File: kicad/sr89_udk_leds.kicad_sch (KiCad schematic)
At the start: 130 parts

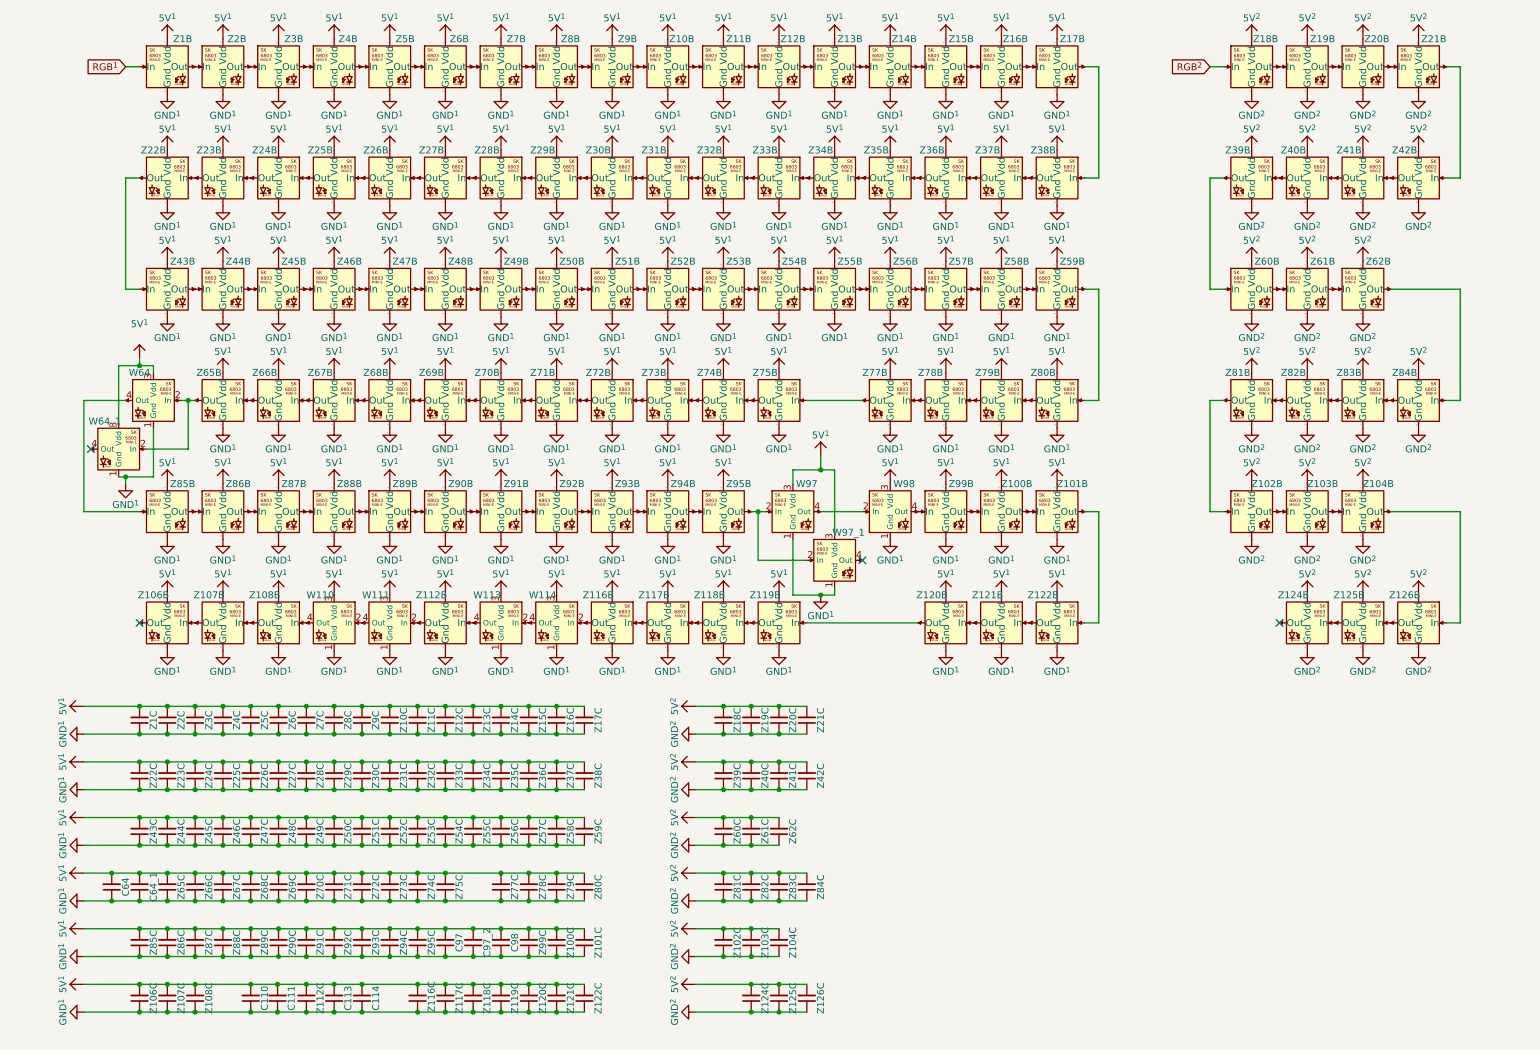
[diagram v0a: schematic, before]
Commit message: routed, but not rules checked
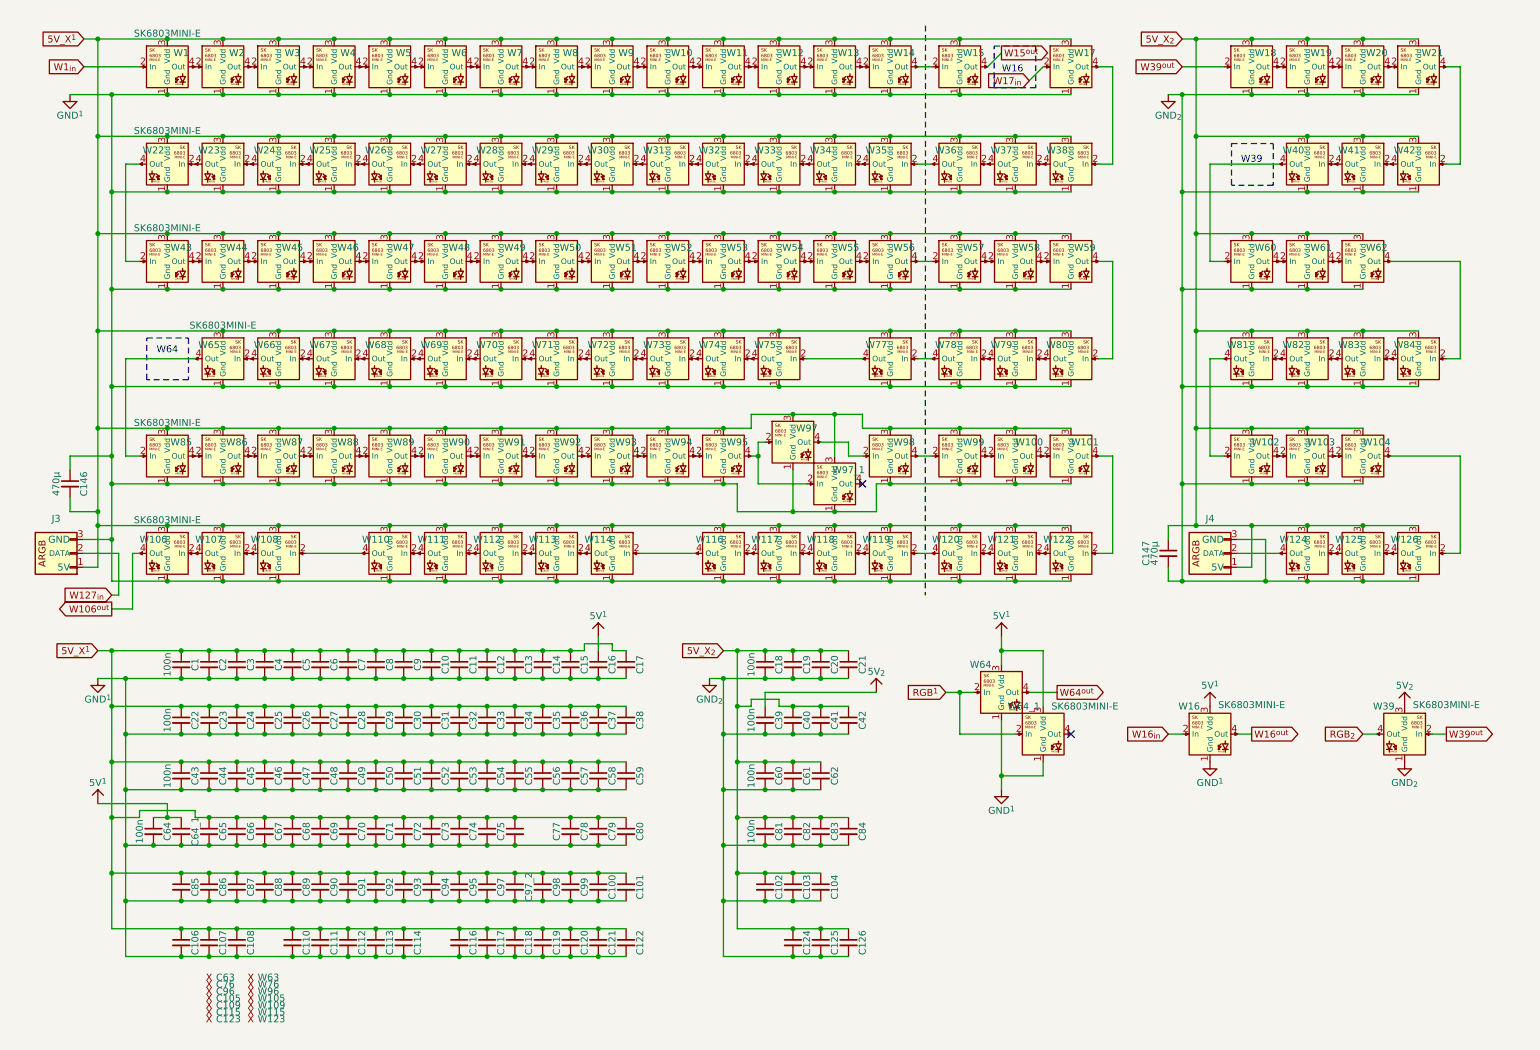
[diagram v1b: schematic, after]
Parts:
- removed Z1, Z10, Z100, Z101, Z102, Z103, Z104, Z106, Z107, Z108, Z11, Z112, Z116, Z117, Z118, Z119, Z12, Z120, Z121, Z122, Z124, Z125, Z126, Z13, Z14, Z15, Z16, Z17, Z18, Z19, Z2, Z20, Z21, Z22, Z23, Z24, Z25, Z26, Z27, Z28, Z29, Z3, Z30, Z31, Z32, Z33, Z34, Z35, Z36, Z37, Z38, Z39, Z4, Z40, Z41, Z42, Z43, Z44, Z45, Z46, Z47, Z48, Z49, Z5, Z50, Z51, Z52, Z53, Z54, Z55, Z56, Z57, Z58, Z59, Z6, Z60, Z61, Z62, Z65, Z66, Z67, Z68, Z69, Z7, Z70, Z71, Z72, Z73, Z74, Z75, Z77, Z78, Z79, Z8, Z80, Z81, Z82, Z83, Z84, Z85, Z86, Z87, Z88, Z89, Z9, Z90, Z91, Z92, Z93, Z94, Z95, Z99: (no value), 0_sr89:Combined_SW_1, symbol 0_sr89:Combined_SW
- added C1, C10, C100, C101, C102, C103, C104, C106, C107, C108, C11, C112, C116, C117, C118, C119, C12, C120, C121, C122, C124, C125, C126, C13, C14, C15, C16, C17, C18, C19, C2, C20, C21, C22, C23, C24, C25, C26, C27, C28, C29, C3, C30, C31, C32, C33, C34, C35, C36, C37, C38, C39, C4, C40, C41, C42, C43, C44, C45, C46, C47, C48, C49, C5, C50, C51, C52, C53, C54, C55, C56, C57, C58, C59, C6, C60, C61, C62, C65, C66, C67, C68, C69, C7, C70, C71, C72, C73, C74, C75, C77, C78, C79, C8, C80, C81, C82, C83, C84, C85, C86, C87, C88, C89, C9, C90, C91, C92, C93, C94, C95, C99: 100n, Capacitor_SMD:C_0402_1005Metric, symbol ts-kicad-lib:C
- added C105, C109, C115, C123, C63, C76, C96, W105, W109, W115, W123, W63, W76, W96: (no value), symbol 0_sr89:X
- added C146, C147: 470µ, Capacitor_SMD:C_0603_1608Metric, symbol ts-kicad-lib:C
- added J3, J4: (no value), ts-kicad-lib:JRAINBOW-5V-ARGB, symbol ts-kicad-lib:ARGB-5V-HEADER
- added W1, W10, W100, W101, W102, W103, W104, W106, W107, W108, W11, W112, W116, W117, W118, W119, W12, W120, W121, W122, W124, W125, W126, W13, W14, W15, W16, W17, W18, W19, W2, W20, W21, W22, W23, W24, W25, W26, W27, W28, W29, W3, W30, W31, W32, W33, W34, W35, W36, W37, W38, W39, W4, W40, W41, W42, W43, W44, W45, W46, W47, W48, W49, W5, W50, W51, W52, W53, W54, W55, W56, W57, W58, W59, W6, W60, W61, W62, W65, W66, W67, W68, W69, W7, W70, W71, W72, W73, W74, W75, W77, W78, W79, W8, W80, W81, W82, W83, W84, W85, W86, W87, W88, W89, W9, W90, W91, W92, W93, W94, W95, W99: SK6803MINI-E, ts-keyboard-lib:SK6803MINI-E, symbol ts-keyboard-lib:SK6803MINI-E
- C64, C64_1: value (none) -> 100n
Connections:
- net 5V^{1}: now also C64.1, C64_1.1, C16.1, W16.3 (Vdd); no longer C110.2, C111.2, C113.2, C114.2, C64.2, C64_1.2, C97.2, C97_2.2, C98.2, W110.3 (Vdd), W111.3 (Vdd), W113.3 (Vdd), W114.3 (Vdd), W97.3 (Vdd), W97_1.3 (Vdd), W98.3 (Vdd)
- net GND^{1}: now also C110.2, C111.2, C113.2, C114.2, C64.2, C64_1.2, C97.2, C97_2.2, C98.2, C1.2, C10.2, C100.2, C101.2, C106.2, C107.2, C108.2, C11.2, C112.2, C116.2, C117.2, C118.2, C119.2, C12.2, C120.2, C121.2, C122.2, C13.2, C14.2, C146.1, C15.2, C16.2, C17.2, C2.2, C22.2, C23.2, C24.2, C25.2, C26.2, C27.2, C28.2, C29.2, C3.2, C30.2, C31.2, C32.2, C33.2, C34.2, C35.2, C36.2, C37.2, C38.2, C4.2, C43.2, C44.2, C45.2, C46.2, C47.2, C48.2, C49.2, C5.2, C50.2, C51.2, C52.2, C53.2, C54.2, C55.2, C56.2, C57.2, C58.2, C59.2, C6.2, C65.2, C66.2, C67.2, C68.2, C69.2, C7.2, C70.2, C71.2, C72.2, C73.2, C74.2, C75.2, C77.2, C78.2, C79.2, C8.2, C80.2, C85.2, C86.2, C87.2, C88.2, C89.2, C9.2, C90.2, C91.2, C92.2, C93.2, C94.2, C95.2, C99.2, J3.3 (GND), W1.1 (Gnd), W10.1 (Gnd), W100.1 (Gnd), W101.1 (Gnd), W106.1 (Gnd), W107.1 (Gnd), W108.1 (Gnd), W11.1 (Gnd), W112.1 (Gnd), W116.1 (Gnd), W117.1 (Gnd), W118.1 (Gnd), W119.1 (Gnd), W12.1 (Gnd), W120.1 (Gnd), W121.1 (Gnd), W122.1 (Gnd), W13.1 (Gnd), W14.1 (Gnd), W15.1 (Gnd), W16.1 (Gnd), W17.1 (Gnd), W2.1 (Gnd), W22.1 (Gnd), W23.1 (Gnd), W24.1 (Gnd), W25.1 (Gnd), W26.1 (Gnd), W27.1 (Gnd), W28.1 (Gnd), W29.1 (Gnd), W3.1 (Gnd), W30.1 (Gnd), W31.1 (Gnd), W32.1 (Gnd), W33.1 (Gnd), W34.1 (Gnd), W35.1 (Gnd), W36.1 (Gnd), W37.1 (Gnd), W38.1 (Gnd), W4.1 (Gnd), W43.1 (Gnd), W44.1 (Gnd), W45.1 (Gnd), W46.1 (Gnd), W47.1 (Gnd), W48.1 (Gnd), W49.1 (Gnd), W5.1 (Gnd), W50.1 (Gnd), W51.1 (Gnd), W52.1 (Gnd), W53.1 (Gnd), W54.1 (Gnd), W55.1 (Gnd), W56.1 (Gnd), W57.1 (Gnd), W58.1 (Gnd), W59.1 (Gnd), W6.1 (Gnd), W65.1 (Gnd), W66.1 (Gnd), W67.1 (Gnd), W68.1 (Gnd), W69.1 (Gnd), W7.1 (Gnd), W70.1 (Gnd), W71.1 (Gnd), W72.1 (Gnd), W73.1 (Gnd), W74.1 (Gnd), W75.1 (Gnd), W77.1 (Gnd), W78.1 (Gnd), W79.1 (Gnd), W8.1 (Gnd), W80.1 (Gnd), W85.1 (Gnd), W86.1 (Gnd), W87.1 (Gnd), W88.1 (Gnd), W89.1 (Gnd), W9.1 (Gnd), W90.1 (Gnd), W91.1 (Gnd), W92.1 (Gnd), W93.1 (Gnd), W94.1 (Gnd), W95.1 (Gnd), W99.1 (Gnd); no longer C110.1, C111.1, C113.1, C114.1, C64.1, C64_1.1, C97.1, C97_2.1, C98.1
- net RGB^{1}: now also W64.2 (In), W64_1.2 (In)
- net at W110.4 (Out): now also W108.2 (In)
- net at W97.2 (In), W97_1.2 (In): now also W95.4 (Out)
- net W64^{out}: now reaches W64.4 (Out)
- net at W114.2 (In): now also W116.4 (Out)
- net at W98.4 (Out): now also W99.2 (In)
- net at W111.2 (In): now also W112.4 (Out)
- net at W113.4 (Out): now also W112.2 (In)
- new net: W100.4 (Out), W101.2 (In)
- new net: W101.4 (Out), W122.2 (In)
- new net: W86.4 (Out), W87.2 (In)
- new net: W87.4 (Out), W88.2 (In)
- new net: W71.2 (In), W72.4 (Out)
- new net: W70.2 (In), W71.4 (Out)
- new net: W60.4 (Out), W61.2 (In)
- new net: W61.4 (Out), W62.2 (In)
- new net: W92.4 (Out), W93.2 (In)
- new net: W93.4 (Out), W94.2 (In)
- new net: W18.4 (Out), W19.2 (In)
- new net: W19.4 (Out), W20.2 (In)
- new net: W79.2 (In), W80.4 (Out)
- new net: W78.2 (In), W79.4 (Out)
- new net: W13.4 (Out), W14.2 (In)
- new net: W14.4 (Out), W15.2 (In)
- new net: W44.4 (Out), W45.2 (In)
- new net: W45.4 (Out), W46.2 (In)
- new net: W20.4 (Out), W21.2 (In)
- new net: W21.4 (Out), W42.2 (In)
- new net: W116.2 (In), W117.4 (Out)
- new net: W90.4 (Out), W91.2 (In)
- new net: W91.4 (Out), W92.2 (In)
- new net: W41.2 (In), W42.4 (Out)
- new net: W10.4 (Out), W11.2 (In)
- new net: W11.4 (Out), W12.2 (In)
- new net: W100.2 (In), W99.4 (Out)
- new net: W102.4 (Out), W103.2 (In)
- new net: W103.4 (Out), W104.2 (In)
- new net: W89.4 (Out), W90.2 (In)
- new net: W67.2 (In), W68.4 (Out)
- new net: W66.2 (In), W67.4 (Out)
- new net: J4.2 (DATA), W124.4 (Out)
- new net: W35.2 (In), W36.4 (Out)
- new net: W34.2 (In), W35.4 (Out)
- new net: W8.4 (Out), W9.2 (In)
- new net: W10.2 (In), W9.4 (Out)
- new net: W57.4 (Out), W58.2 (In)
- new net: W58.4 (Out), W59.2 (In)
- new net: W17.4 (Out), W38.2 (In)
- new net: W107.2 (In), W108.4 (Out)
- new net: W106.2 (In), W107.4 (Out)
- new net: W53.4 (Out), W54.2 (In)
- new net: W54.4 (Out), W55.2 (In)
- new net: W25.2 (In), W26.4 (Out)
- new net: W24.2 (In), W25.4 (Out)
- new net: W121.2 (In), W122.4 (Out)
- new net: W81.2 (In), W82.4 (Out)
- new net: W102.2 (In), W81.4 (Out)
- new net: W5.4 (Out), W6.2 (In)
- new net: W6.4 (Out), W7.2 (In)
- new net: W37.2 (In), W38.4 (Out)
- new net: W125.2 (In), W126.4 (Out)
- new net: W124.2 (In), W125.4 (Out)
- new net: W46.4 (Out), W47.2 (In)
- new net: W55.4 (Out), W56.2 (In)
- new net: W47.4 (Out), W48.2 (In)
- new net: W48.4 (Out), W49.2 (In)
- new net: W77.2 (In), W78.4 (Out)
- new net: W31.2 (In), W32.4 (Out)
- new net: W30.2 (In), W31.4 (Out)
- new net: W94.4 (Out), W95.2 (In)
- new net: W27.2 (In), W28.4 (Out)
- new net: W26.2 (In), W27.4 (Out)
- new net: W69.2 (In), W70.4 (Out)
- new net: W68.2 (In), W69.4 (Out)
- new net: W2.4 (Out), W3.2 (In)
- new net: W3.4 (Out), W4.2 (In)
- new net: W120.2 (In), W121.4 (Out)
- new net: W119.2 (In), W120.4 (Out)
- new net: W62.4 (Out), W84.2 (In)
- new net: W83.2 (In), W84.4 (Out)
- new net: W43.4 (Out), W44.2 (In)
- new net: W23.2 (In), W24.4 (Out)
- new net: W22.2 (In), W23.4 (Out)
- new net: W4.4 (Out), W5.2 (In)
- new net: W88.4 (Out), W89.2 (In)
- new net: W73.2 (In), W74.4 (Out)
- new net: W72.2 (In), W73.4 (Out)
- new net: W118.2 (In), W119.4 (Out)
- new net: W82.2 (In), W83.4 (Out)
- new net: W33.2 (In), W34.4 (Out)
- new net: W59.4 (Out), W80.2 (In)
- new net: W22.4 (Out), W43.2 (In)
- new net: W117.2 (In), W118.4 (Out)
- new net: W56.4 (Out), W57.2 (In)
- new net: W40.2 (In), W41.4 (Out)
- new net: W40.4 (Out), W60.2 (In)
- new net: W49.4 (Out), W50.2 (In)
- new net: W50.4 (Out), W51.2 (In)
- new net: W65.2 (In), W66.4 (Out)
- new net: W28.2 (In), W29.4 (Out)
- new net: W51.4 (Out), W52.2 (In)
- new net: W85.4 (Out), W86.2 (In)
- new net: W29.2 (In), W30.4 (Out)
- new net: W32.2 (In), W33.4 (Out)
- new net: W52.4 (Out), W53.2 (In)
- new net: W12.4 (Out), W13.2 (In)
- new net: W36.2 (In), W37.4 (Out)
- new net: W7.4 (Out), W8.2 (In)
- new net: W65.4 (Out), W85.2 (In)
- new net: W1.4 (Out), W2.2 (In)
- new net: W74.2 (In), W75.4 (Out)
- new net: W104.4 (Out), W126.2 (In)
- new net: W75.2 (In), W77.4 (Out)
- new net 5V_X^{1}: C1.1, C10.1, C100.1, C101.1, C106.1, C107.1, C108.1, C11.1, C110.1, C111.1, C112.1, C113.1, C114.1, C116.1, C117.1, C118.1, C119.1, C12.1, C120.1, C121.1, C122.1, C13.1, C14.1, C146.2, C15.1, C17.1, C2.1, C22.1, C23.1, C24.1, C25.1, C26.1, C27.1, C28.1, C29.1, C3.1, C30.1, C31.1, C32.1, C33.1, C34.1, C35.1, C36.1, C37.1, C38.1, C4.1, C43.1, C44.1, C45.1, C46.1, C47.1, C48.1, C49.1, C5.1, C50.1, C51.1, C52.1, C53.1, C54.1, C55.1, C56.1, C57.1, C58.1, C59.1, C6.1, C65.1, C66.1, C67.1, C68.1, C69.1, C7.1, C70.1, C71.1, C72.1, C73.1, C74.1, C75.1, C77.1, C78.1, C79.1, C8.1, C80.1, C85.1, C86.1, C87.1, C88.1, C89.1, C9.1, C90.1, C91.1, C92.1, C93.1, C94.1, C95.1, C97.1, C97_2.1, C98.1, C99.1, J3.1 (5V), W1.3 (Vdd), W10.3 (Vdd), W100.3 (Vdd), W101.3 (Vdd), W106.3 (Vdd), W107.3 (Vdd), W108.3 (Vdd), W11.3 (Vdd), W110.3 (Vdd), W111.3 (Vdd), W112.3 (Vdd), W113.3 (Vdd), W114.3 (Vdd), W116.3 (Vdd), W117.3 (Vdd), W118.3 (Vdd), W119.3 (Vdd), W12.3 (Vdd), W120.3 (Vdd), W121.3 (Vdd), W122.3 (Vdd), W13.3 (Vdd), W14.3 (Vdd), W15.3 (Vdd), W17.3 (Vdd), W2.3 (Vdd), W22.3 (Vdd), W23.3 (Vdd), W24.3 (Vdd), W25.3 (Vdd), W26.3 (Vdd), W27.3 (Vdd), W28.3 (Vdd), W29.3 (Vdd), W3.3 (Vdd), W30.3 (Vdd), W31.3 (Vdd), W32.3 (Vdd), W33.3 (Vdd), W34.3 (Vdd), W35.3 (Vdd), W36.3 (Vdd), W37.3 (Vdd), W38.3 (Vdd), W4.3 (Vdd), W43.3 (Vdd), W44.3 (Vdd), W45.3 (Vdd), W46.3 (Vdd), W47.3 (Vdd), W48.3 (Vdd), W49.3 (Vdd), W5.3 (Vdd), W50.3 (Vdd), W51.3 (Vdd), W52.3 (Vdd), W53.3 (Vdd), W54.3 (Vdd), W55.3 (Vdd), W56.3 (Vdd), W57.3 (Vdd), W58.3 (Vdd), W59.3 (Vdd), W6.3 (Vdd), W65.3 (Vdd), W66.3 (Vdd), W67.3 (Vdd), W68.3 (Vdd), W69.3 (Vdd), W7.3 (Vdd), W70.3 (Vdd), W71.3 (Vdd), W72.3 (Vdd), W73.3 (Vdd), W74.3 (Vdd), W75.3 (Vdd), W77.3 (Vdd), W78.3 (Vdd), W79.3 (Vdd), W8.3 (Vdd), W80.3 (Vdd), W85.3 (Vdd), W86.3 (Vdd), W87.3 (Vdd), W88.3 (Vdd), W89.3 (Vdd), W9.3 (Vdd), W90.3 (Vdd), W91.3 (Vdd), W92.3 (Vdd), W93.3 (Vdd), W94.3 (Vdd), W95.3 (Vdd), W97.3 (Vdd), W97_1.3 (Vdd), W98.3 (Vdd), W99.3 (Vdd)
- new net 5V_X_{2}: C102.1, C103.1, C104.1, C124.1, C125.1, C126.1, C147.1, C18.1, C19.1, C20.1, C21.1, C40.1, C41.1, C42.1, C60.1, C61.1, C62.1, C81.1, C82.1, C83.1, C84.1, J4.1 (5V), W102.3 (Vdd), W103.3 (Vdd), W104.3 (Vdd), W124.3 (Vdd), W125.3 (Vdd), W126.3 (Vdd), W18.3 (Vdd), W19.3 (Vdd), W20.3 (Vdd), W21.3 (Vdd), W40.3 (Vdd), W41.3 (Vdd), W42.3 (Vdd), W60.3 (Vdd), W61.3 (Vdd), W62.3 (Vdd), W81.3 (Vdd), W82.3 (Vdd), W83.3 (Vdd), W84.3 (Vdd)
- new net 5V_{2}: C39.1, W39.3 (Vdd)
- new net GND_{2}: C102.2, C103.2, C104.2, C124.2, C125.2, C126.2, C147.2, C18.2, C19.2, C20.2, C21.2, C39.2, C40.2, C41.2, C42.2, C60.2, C61.2, C62.2, C81.2, C82.2, C83.2, C84.2, J4.3 (GND), W102.1 (Gnd), W103.1 (Gnd), W104.1 (Gnd), W124.1 (Gnd), W125.1 (Gnd), W126.1 (Gnd), W18.1 (Gnd), W19.1 (Gnd), W20.1 (Gnd), W21.1 (Gnd), W39.1 (Gnd), W40.1 (Gnd), W41.1 (Gnd), W42.1 (Gnd), W60.1 (Gnd), W61.1 (Gnd), W62.1 (Gnd), W81.1 (Gnd), W82.1 (Gnd), W83.1 (Gnd), W84.1 (Gnd)
- new net RGB_{2}: W39.4 (Out)
- new net W106^{out}: W106.4 (Out)
- new net W127_{in}: J3.2 (DATA)
- new net W15^{out}: W15.4 (Out)
- new net W16^{out}: W16.4 (Out)
- new net W16_{in}: W16.2 (In)
- new net W17_{in}: W17.2 (In)
- new net W1_{in}: W1.2 (In)
- new net W39^{out}: W18.2 (In), W39.2 (In)
- no-connect marks 4 -> 2
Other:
- note added: "W16"
- note added: "W39"
- note added: "W64"
- moved on the sheet: C110, C111, C113, C114, C64, C64_1, C97, C97_2, C98, W110, W111, W113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
